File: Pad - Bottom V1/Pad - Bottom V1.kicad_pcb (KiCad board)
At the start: 2 copper layers, 72.9 x 23 mm, 3 parts, among them J1 B2B-XH-A

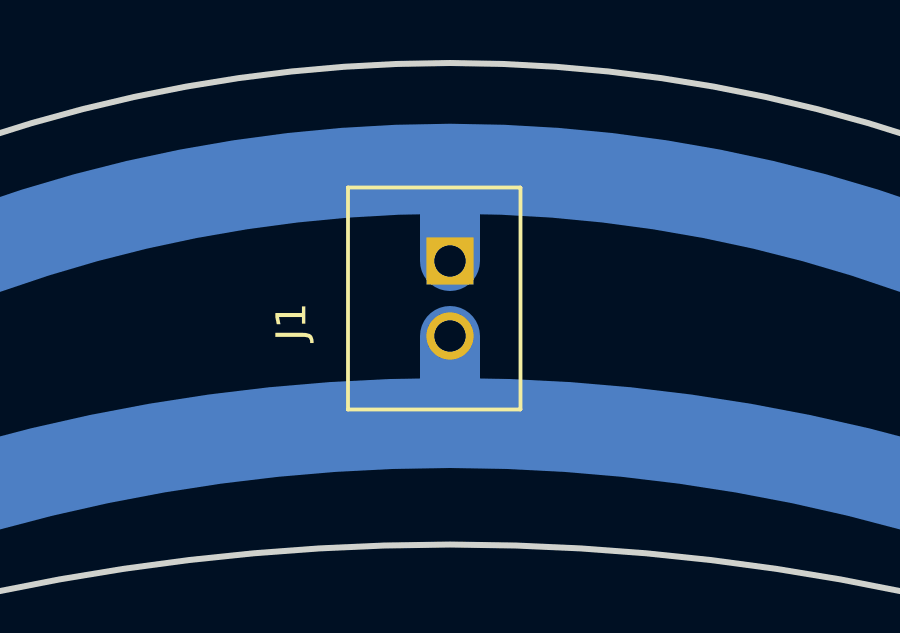
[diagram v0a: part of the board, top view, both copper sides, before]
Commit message: Made top board the pogo board and bulkhead the pad board.
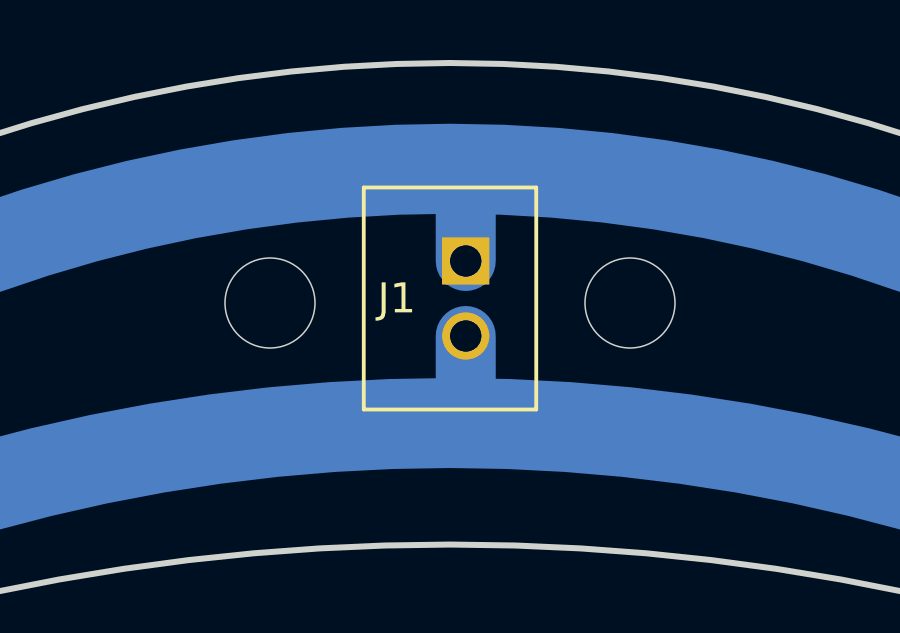
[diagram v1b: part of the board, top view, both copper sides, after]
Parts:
- moved J1 0.53 mm to (149.2, 64.1)
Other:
- outline, holes or cut-outs redrawn
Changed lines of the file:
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@@
 	(footprint "B2B-XH-A:B2B-XH-A"
 		(layer "F.Cu")
-		(at 148.724999 64.1 90)
+		(at 149.25 64.1 90)
 		(property "Reference" "J1"
-			(at -0.775 -4.76 90)
+			(at 0 -1.774999 180)
 			(layer "F.SilkS")
 			(effects
@@
 		(net 1)
 	)
-	(gr_arc
-		(start 122.879886 68.089441)
-		(mid 149.250076 59.775)
-		(end 175.620239 68.089529)
-		(stroke
-			(width 3)
-			(type default)
-		)
+	(gr_circle
+		(center 170.35 64.95)
+		(end 171.4 64.95)
+		(stroke
+			(width 0)
+			(type solid)
+		)
+		(fill solid)
 		(layer "B.Mask")
 	)
-	(gr_arc
-		(start 126.329351 73.015805)
-		(mid 149.250062 68.250001)
-		(end 172.170758 73.015881)
-		(stroke
-			(width 3)
-			(type default)
-		)
+	(gr_circle
+		(center 127.95 65)
+		(end 129 65)
+		(stroke
+			(width 0)
+			(type solid)
+		)
+		(fill solid)
 		(layer "B.Mask")
+	)
+	(gr_circle
+		(center 149.25 68.25)
+		(end 150.3 68.25)
+		(stroke
+			(width 0)
+			(type solid)
+		)
+		(fill solid)
+		(layer "B.Mask")
+	)
+	(gr_circle
+		(center 149.25 59.8)
+		(end 150.3 59.8)
+		(stroke
+			(width 0)
+			(type solid)
+		)
+		(fill solid)
+		(layer "B.Mask")
+	)
+	(gr_circle
+		(center 166 70.75)
+		(end 167.05 70.75)
+		(stroke
+			(width 0)
+			(type solid)
+		)
+		(fill solid)
+		(layer "B.Mask")
+	)
+	(gr_circle
+		(center 132.5 70.75)
+		(end 133.55 70.75)
+		(stroke
+			(width 0)
+			(type solid)
+		)
+		(fill solid)
+		(layer "B.Mask")
+	)
+	(gr_line
+		(start 149.25 105.75)
+		(end 143.25 64.25)
+		(stroke
+			(width 0.1)
+			(type default)
+		)
+		(layer "Dwgs.User")
+	)
+	(gr_line
+		(start 149.250056 72.301328)
+		(end 149.250083 56.25)
+		(stroke
+			(width 0.1)
+			(type default)
+		)
+		(layer "Dwgs.User")
+	)
+	(gr_line
+		(start 149.25007 64.275664)
+		(end 155.25 64.25)
+		(stroke
+			(width 0.1)
+			(type default)
+		)
+		(layer "Dwgs.User")
+	)
+	(gr_circle
+		(center 149.25 105.75)
+		(end 149.5 105.75)
+		(stroke
+			(width 0.2)
+			(type default)
+		)
+		(fill none)
+		(layer "Dwgs.User")
+	)
+	(gr_line
+		(start 149.25007 64.275664)
+		(end 143.25 64.25)
+		(stroke
+			(width 0.1)
+			(type default)
+		)
+		(layer "Dwgs.User")
 	)
 	(gr_arc
@@
 		(layer "Edge.Cuts")
 	)
+	(gr_circle
+		(center 155.25 64.25)
+		(end 156.75 64.25)
+		(stroke
+			(width 0.05)
+			(type default)
+		)
+		(fill none)
+		(layer "Edge.Cuts")
+	)
 	(gr_arc
 		(start 184.251844 70.748273)
@@
 		(layer "Edge.Cuts")
 	)
+	(gr_circle
+		(center 143.25 64.25)
+		(end 143.25 65.75)
+		(stroke
+			(width 0.05)
+			(type default)
+		)
+		(fill none)
+		(layer "Edge.Cuts")
+	)
+	(dimension
+		(type aligned)
+		(layer "Dwgs.User")
+		(pts
+			(xy 149.250056 72.301328) (xy 149.250083 56.25)
+		)
+		(height 0)
+		(gr_text "16.0513 mm"
+			(at 148.10007 64.275662 89.99990005)
+			(layer "Dwgs.User")
+			(effects
+				(font
+					(size 1 1)
+					(thickness 0.15)
+				)
+			)
+		)
+		(format
+			(prefix "")
+			(suffix "")
+			(units 3)
+			(units_format 1)
+			(precision 4)
+		)
+		(style
+			(thickness 0.1)
+			(arrow_length 1.27)
+			(text_position_mode 0)
+			(extension_height 0.58642)
+			(extension_offset 0.5) keep_text_aligned)
+	)
 	(segment
-		(start 149.25 65.35)
-		(end 149.25 68.249939)
+		(start 149.250062 68.250001)
+		(end 149.775001 67.725062)
 		(width 2)
 		(layer "B.Cu")
@@
 	)
 	(segment
-		(start 149.25 68.249939)
-		(end 149.250062 68.250001)
+		(start 149.775001 67.725062)
+		(end 149.775001 65.35)
 		(width 2)
 		(layer "B.Cu")
@@
 	)
 	(segment
-		(start 149.25 62.85)
-		(end 149.25 59.76)
+		(start 149.775001 62.85)
+		(end 149.775001 60.299925)
 		(width 2)
 		(layer "B.Cu")
@@
 	(segment
 		(start 149.25 59.775076)
+		(end 149.25 59.774969)
+		(width 2.1)
+		(layer "B.Cu")
+		(net 2)
+	)
+	(segment
+		(start 149.775001 60.299925)
 		(end 149.250076 59.775)
 		(width 2)

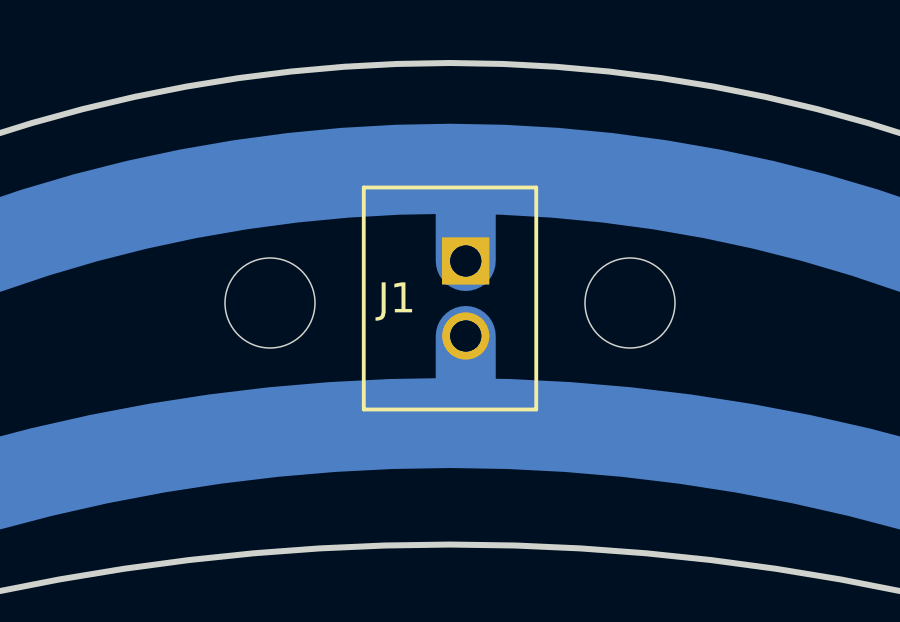
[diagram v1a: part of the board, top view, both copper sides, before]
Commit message: Fixed alingment pin placement and sizing for pogo and pad boards.
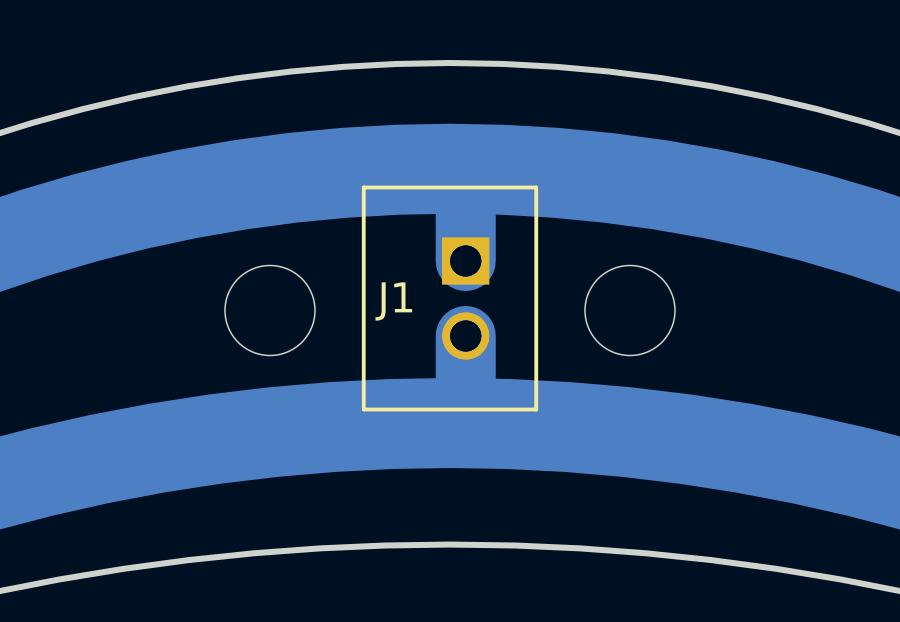
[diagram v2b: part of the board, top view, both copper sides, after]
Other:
- outline, holes or cut-outs redrawn
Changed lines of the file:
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@@
 	)
 	(gr_circle
-		(center 155.25 64.25)
-		(end 156.75 64.25)
+		(center 155.25 64.5)
+		(end 156.75 64.5)
 		(stroke
 			(width 0.05)
@@
 	)
 	(gr_circle
-		(center 143.25 64.25)
-		(end 143.25 65.75)
+		(center 143.25 64.5)
+		(end 144.75 64.5)
 		(stroke
 			(width 0.05)

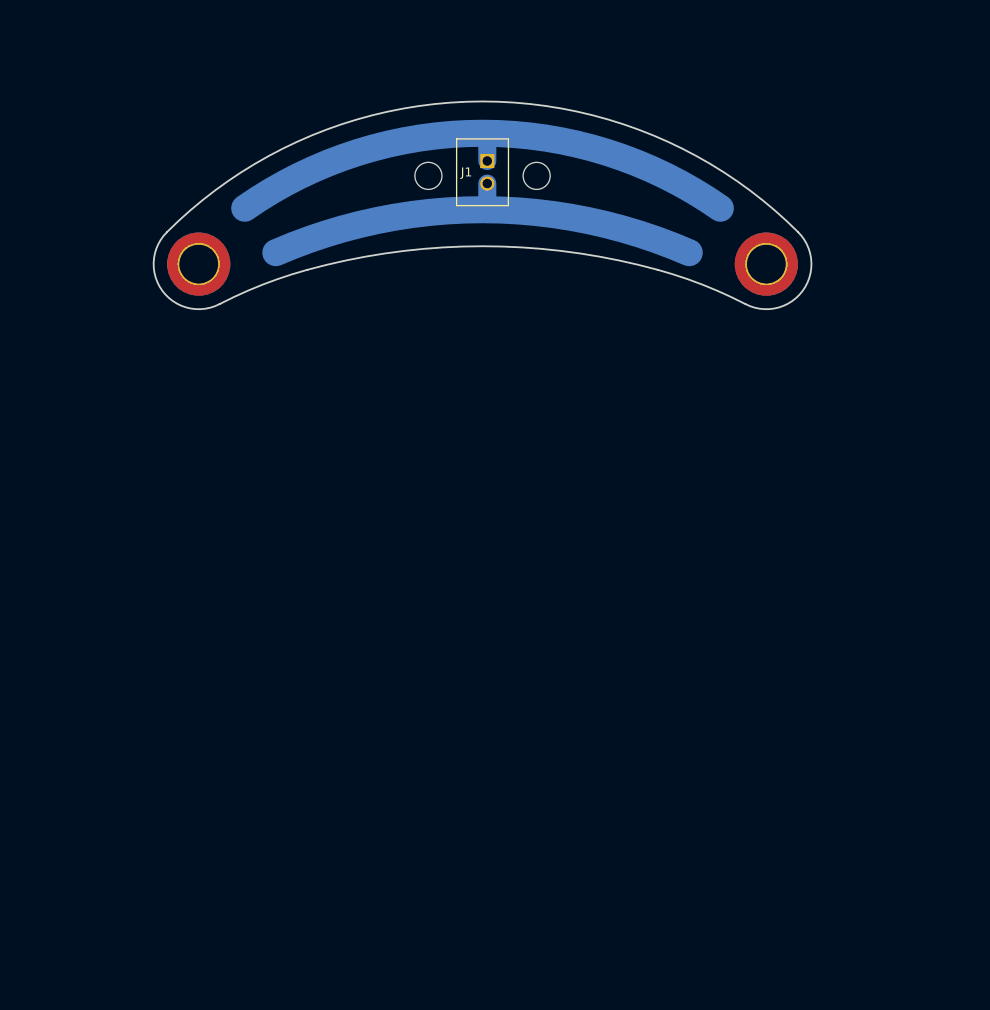
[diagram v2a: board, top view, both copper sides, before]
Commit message: Finally fixed the issues with folder and file naming.
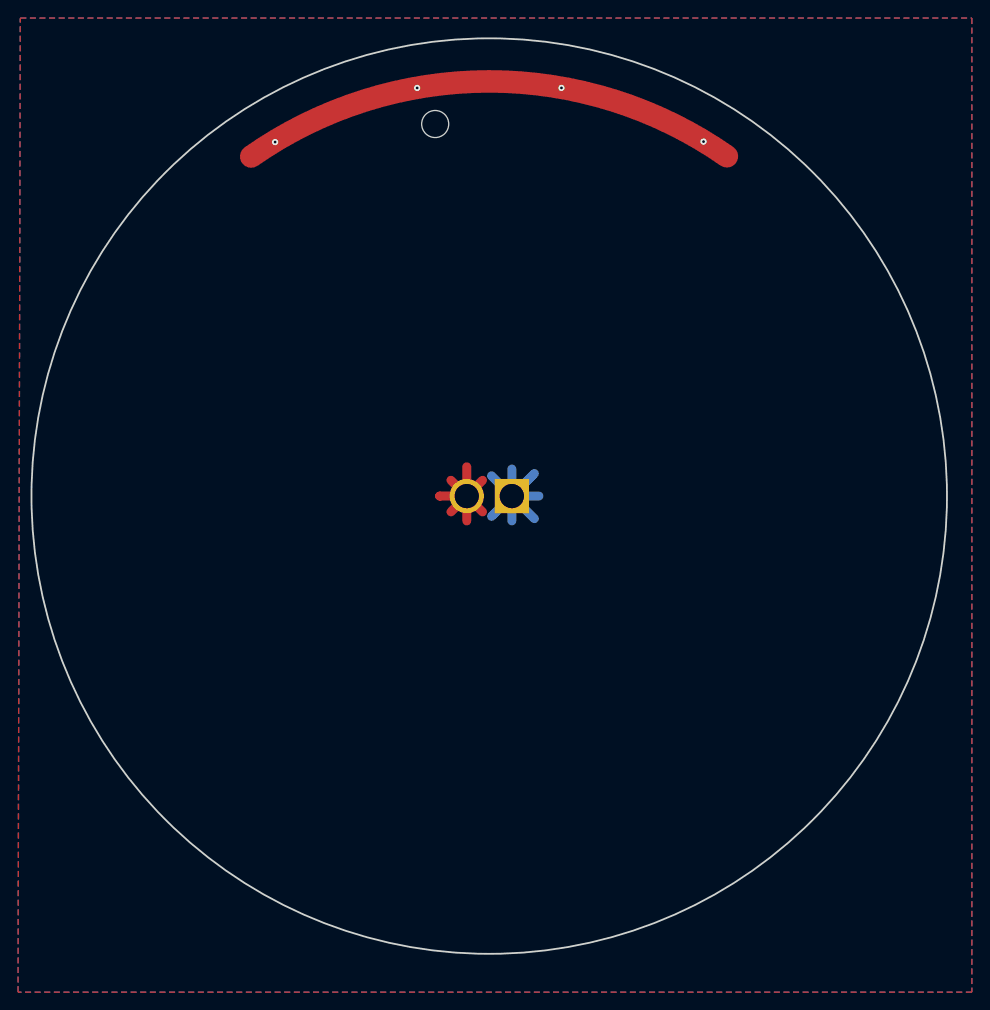
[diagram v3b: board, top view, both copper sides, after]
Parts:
- removed REF** (x2): MountingHole_4.3mm_M4_Pad_TopBottom, MountingHole:MountingHole_4.3mm_M4_Pad_TopBottom
- J1: value B2B-XH-A -> Conn_01x02_Socket; footprint B2B-XH-A:B2B-XH-A -> Connector_AMASS:AMASS_XT30U-M_1x02_P5.0mm_Vertical; moved to B.Cu
- moved J1 36.0 mm to (152.5, 100.0), turned to 180 degrees
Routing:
- net GND: track 3.29 -> 22.2 mm, vias 0 -> 4
- net +9V: track 3.12 -> 18.9 mm
- added copper zone on F.Cu, net +9V
- added copper zone on B.Cu, net GND
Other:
- board size 72.9 x 23 mm -> 101.5 x 101.5 mm
